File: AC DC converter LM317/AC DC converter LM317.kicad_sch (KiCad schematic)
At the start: 19 parts, among them J1 Screw_Terminal_01x02, J2 Screw_Terminal_01x02, U1 LM317_TO-220

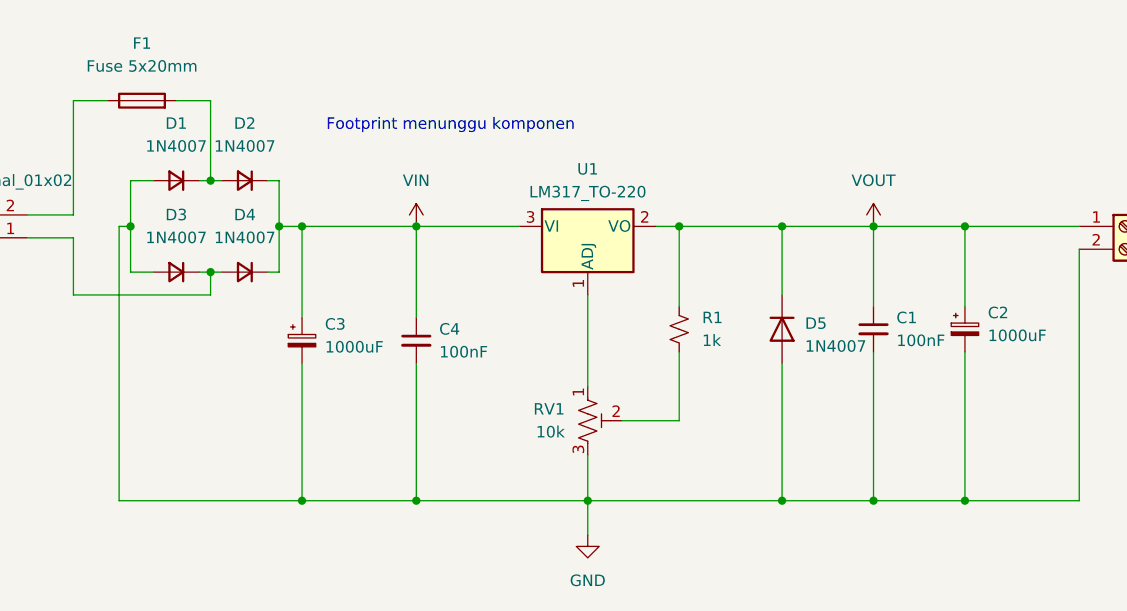
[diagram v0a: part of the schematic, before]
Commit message: minor update
Change R1 Value (1k to 240)
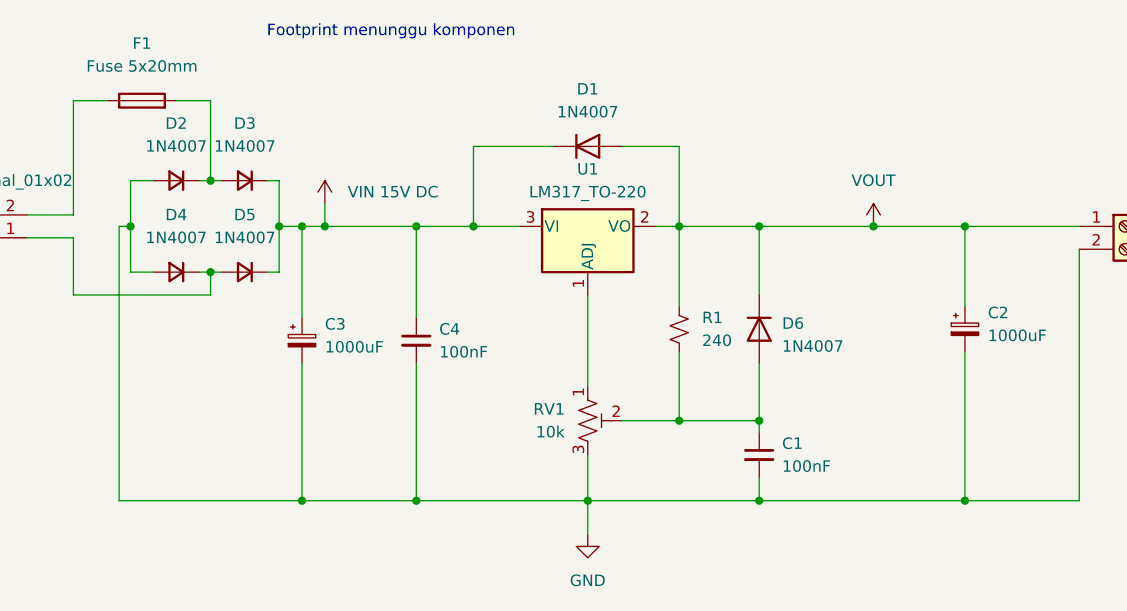
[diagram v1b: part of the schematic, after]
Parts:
- added D1: 1N4007, Diode_THT:D_DO-41_SOD81_P10.16mm_Horizontal, symbol Diode:1N4007
- D2: renamed from D1; footprint Diode_THT:D_5W_P12.70mm_Horizontal -> Diode_THT:D_DO-41_SOD81_P10.16mm_Horizontal
- D3: renamed from D2; footprint Diode_THT:D_5W_P12.70mm_Horizontal -> Diode_THT:D_DO-41_SOD81_P10.16mm_Horizontal
- D4: renamed from D3; footprint Diode_THT:D_5W_P12.70mm_Horizontal -> Diode_THT:D_DO-41_SOD81_P10.16mm_Horizontal
- D5: renamed from D4; footprint Diode_THT:D_5W_P12.70mm_Horizontal -> Diode_THT:D_DO-41_SOD81_P10.16mm_Horizontal
- R1: value 1k -> 240
- renumbered D5 to D6
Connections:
- net GND: no longer D6.2 (A)
- net VOUT: now also D1.2 (A); no longer C1.1
- net at R1.2, RV1.2: now also C1.1, D6.2 (A)
- net VIN renamed VIN 15V DC
- net VIN 15V DC: now also D1.1 (K)
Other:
- moved on the sheet: C1, D6

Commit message: Finished PCB and Schematic
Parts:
- removed C1: 100nF, symbol Device:C_Small
- removed D1, D6: 1N4007, Diode_THT:D_DO-41_SOD81_P10.16mm_Horizontal, symbol Diode:1N4007
- removed D2, D3, D4, D5: 1N4007, Diode_THT:D_DO-41_SOD81_P10.16mm_Horizontal, symbol Device:D_Small
- removed RV1: 10k, symbol Device:R_Potentiometer_Trim_US
- added C3: 100nF, Capacitor_THT:C_Rect_L7.0mm_W2.5mm_P5.00mm, symbol Device:C_Small
- added D1, D2, D3, D4: 1N4007, Diode_THT:D_DO-41_SOD81_P10.16mm_Horizontal, symbol Device:D_45deg
- added J3: Conn_01x04_Socket, Connector_PinHeader_2.54mm:PinHeader_1x04_P2.54mm_Vertical, symbol Connector:Conn_01x04_Socket
- added J4: Conn_01x02_Pin, Connector_PinHeader_2.54mm:PinHeader_1x02_P2.54mm_Vertical, symbol Connector:Conn_01x02_Pin
- added R2: 510, Resistor_THT:R_Axial_DIN0207_L6.3mm_D2.5mm_P7.62mm_Horizontal, symbol Device:R_Small_US
- added R3: 220, Resistor_THT:R_Axial_DIN0207_L6.3mm_D2.5mm_P7.62mm_Horizontal, symbol Device:R_Small_US
- added RV1: 10k, Potentiometer_THT:Potentiometer_Bourns_3296W_Vertical, symbol Device:R_Potentiometer_Small
- C1: renamed from C3; footprint (none) -> Capacitor_THT:CP_Radial_D10.0mm_P5.00mm
- C2: renamed from C4; footprint (none) -> Capacitor_THT:C_Rect_L7.0mm_W2.5mm_P5.00mm
- C4: renamed from C2; footprint (none) -> Capacitor_THT:CP_Radial_D10.0mm_P5.00mm
- H1, H2, H3, H4: footprint MountingHole:MountingHole_2.7mm_M2.5_DIN965_Pad -> MountingHole:MountingHole_3.2mm_M3_Pad
- J1: renamed from J2; value Screw_Terminal_01x02 -> Input AC; footprint TerminalBlock_Phoenix:TerminalBlock_Phoenix_MKDS-1,5-2_1x02_P5.00mm_Horizontal -> TerminalBlock:TerminalBlock_bornier-2_P5.08mm
- J2: renamed from J1; value Screw_Terminal_01x02 -> Output; footprint TerminalBlock_Phoenix:TerminalBlock_Phoenix_MKDS-1,5-2_1x02_P5.00mm_Horizontal -> TerminalBlock:TerminalBlock_bornier-2_P5.08mm
- R1: footprint (none) -> Resistor_THT:R_Axial_DIN0207_L6.3mm_D2.5mm_P7.62mm_Horizontal
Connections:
- net GND: now also C3.2, D1.2 (A), D3.2 (A), J4.1 (Pin_1), R3.2, RV1.2, RV1.3
- net VIN 15V DC: now also D2.1 (K), D4.1 (K)
- net VOUT: now also C3.1, J4.2 (Pin_2)
- net at J1.1 (Pin_1): now also F1.1
- net at F1.2: now also D1.1 (K), D2.2 (A)
- net at R1.2: now also J3.4 (Pin_4), R2.1
- net at J1.2 (Pin_2): now also D3.1 (K), D4.2 (A); no longer F1.1
- net at U1.1 (ADJ): now also J3.3 (Pin_3)
- new net: R2.2, R3.1
- new net: J3.1 (Pin_1), J3.2 (Pin_2), RV1.1
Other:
- note removed: "Footprint menunggu komponen"
- title: (none) -> AC-DC Converter Adjustable / Fixed 5V option
- moved on the sheet: C1, C2, C4, F1, H1, J1, J2, R1, U1
